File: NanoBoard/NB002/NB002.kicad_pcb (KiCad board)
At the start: 2 copper layers, 22 x 72.8 mm, 18 parts, among them M1 Motor_DC, SW1 SW, SW2 Limit Switch, U2 MS583730BA01-50, U4 XiaoESP32C3

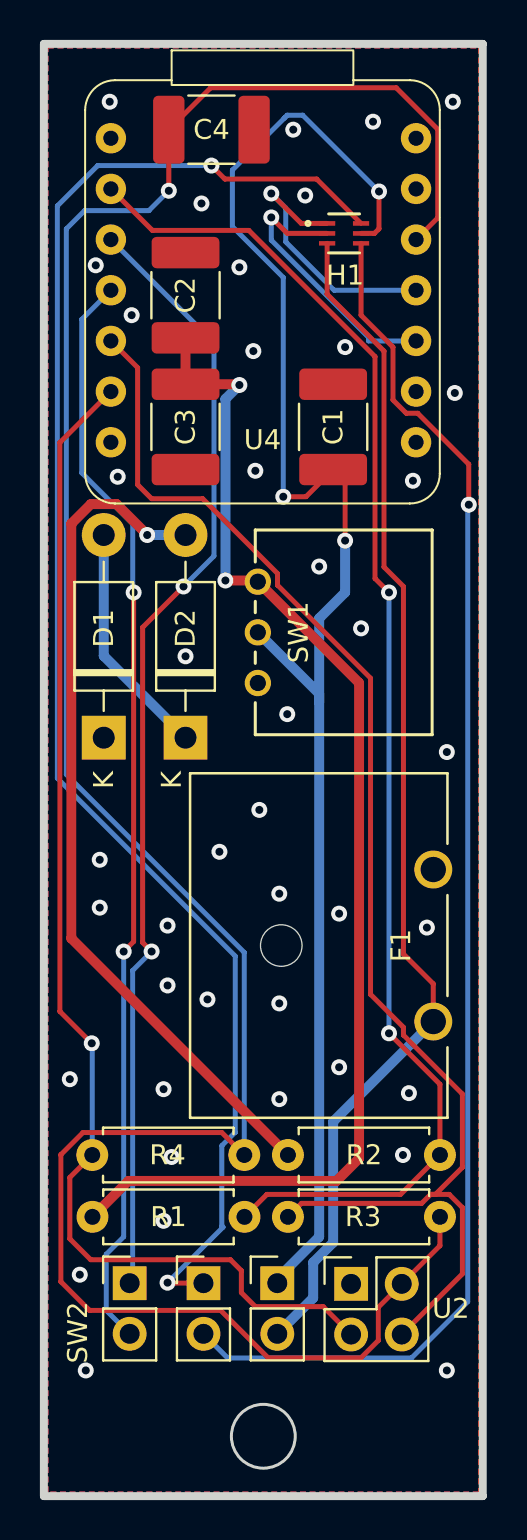
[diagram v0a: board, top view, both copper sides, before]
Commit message: Full Rework of NanoBoard Libraries, Updated Final Version of NB101
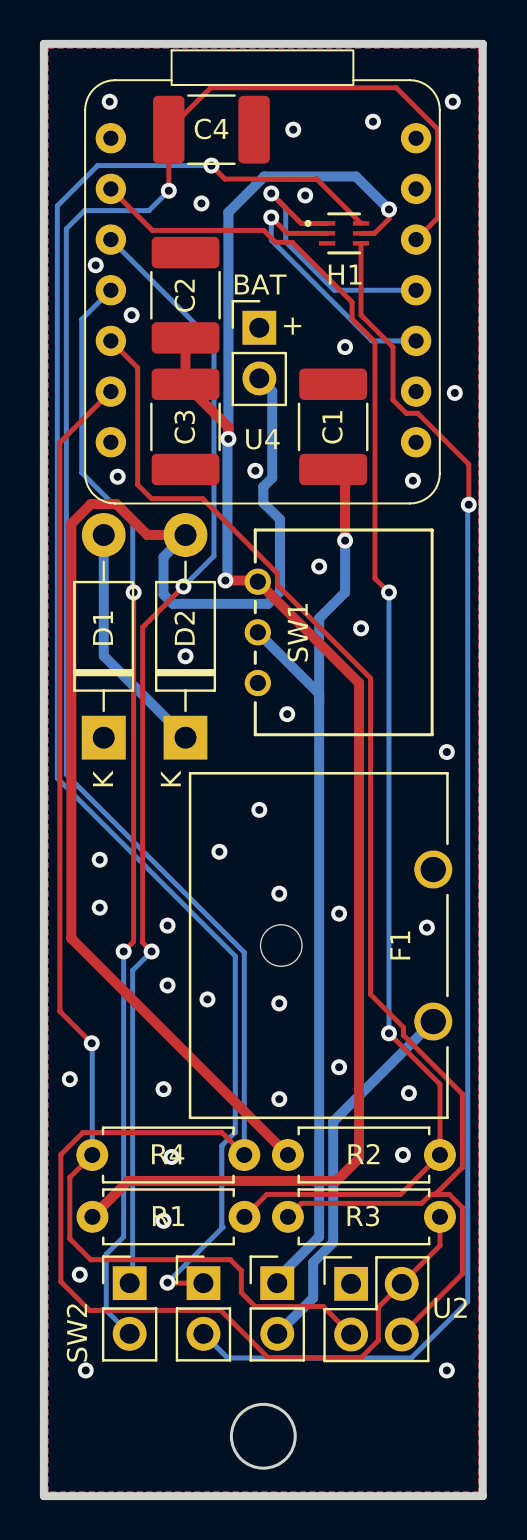
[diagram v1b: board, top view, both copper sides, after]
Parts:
- added BAT: PinHeader_1x02_P2.54mm_Vertical, Connector_PinHeader_2.54mm:PinHeader_1x02_P2.54mm_Vertical, F.Cu at (125.4, 87.3)
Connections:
- H1 pad 3: Net-(B4--) -> Net-(D1-K)
- H1 pad 5: Net-(B4-+) -> Net-(HBridge1-VDD)
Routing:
- net Net-(B4--): track 60.1 -> 18.9 mm
- net Net-(B4-+): track 80.5 -> 47.0 mm, vias 3 -> 1
- net Net-(D2-A): track 42.9 -> 64.1 mm, vias 1 -> 0
- net Net-(HBridge1-VDD): track 62.4 -> 83.4 mm, vias 2 -> 3
- net Net-(U4-D0): track 69.2 -> 70.1 mm
- net Net-(D1-K): vias 42 -> 40
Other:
- board text added: "+"
